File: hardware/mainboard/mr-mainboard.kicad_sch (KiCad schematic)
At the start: 5 parts

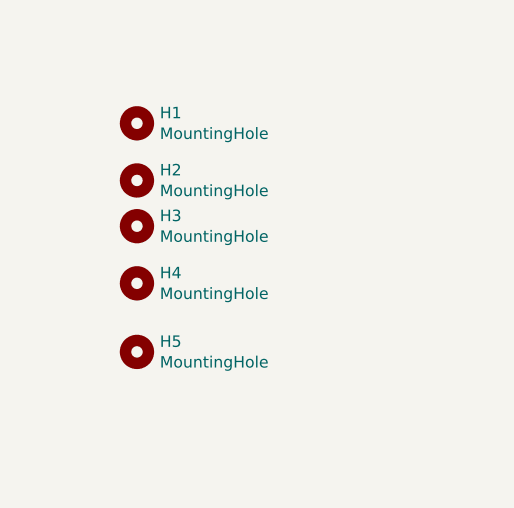
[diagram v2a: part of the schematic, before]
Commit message: Mainboard mechanical tweaks
Signed-off-by: gatecat <gatecat@ds0.me>
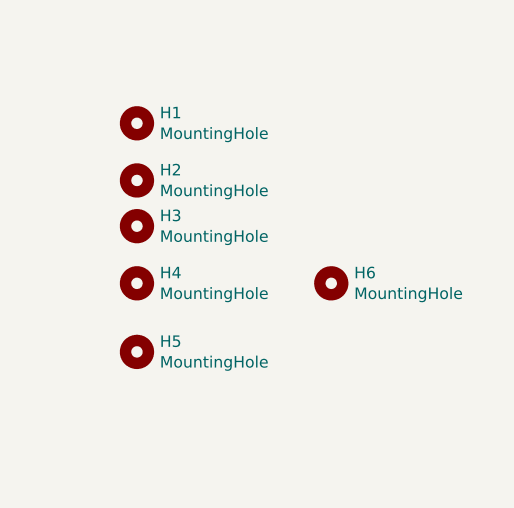
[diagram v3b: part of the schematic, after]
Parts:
- added H6: MountingHole, MountingHole:MountingHole_2.7mm_M2.5, symbol Mechanical:MountingHole
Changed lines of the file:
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@@
+    )
+  )
+  (symbol (lib_id "Mechanical:MountingHole") (at 237.49 81.28 0) (unit 1)
+    (in_bom yes) (on_board yes)
+    (property "Reference" "H6" (id 0) (at 240.0301 80.1306 0)
+      (effects (font (size 1.27 1.27)) (justify left))
+    )
+    (property "Value" "MountingHole" (id 1) (at 240.0301 82.4293 0)
+      (effects (font (size 1.27 1.27)) (justify left))
+    )
+    (property "Footprint" "MountingHole:MountingHole_2.7mm_M2.5" (id 2) (at 237.49 81.28 0)
+      (effects (font (size 1.27 1.27)) hide)
+    )
+    (property "Datasheet" "~" (id 3) (at 237.49 81.28 0)
+      (effects (font (size 1.27 1.27)) hide)
     )
   )
@@
       (reference "H5") (unit 1) (value "MountingHole") (footprint "meowality:9774025151R")
     )
+    (path "/b05d6d30-eaf6-4bdd-a182-1d6bf743d222"
+      (reference "H6") (unit 1) (value "MountingHole") (footprint "MountingHole:MountingHole_2.7mm_M2.5")
+    )
     (path "/7dd540ee-d364-4396-a5ce-94105f298dc9/4dd6052b-4c44-4337-bca1-1febcef57c4e"
